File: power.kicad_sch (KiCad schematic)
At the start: 45 parts, among them U2 BQ25176J, U3 TPS61201DRC, U4 BQ51050BRHL

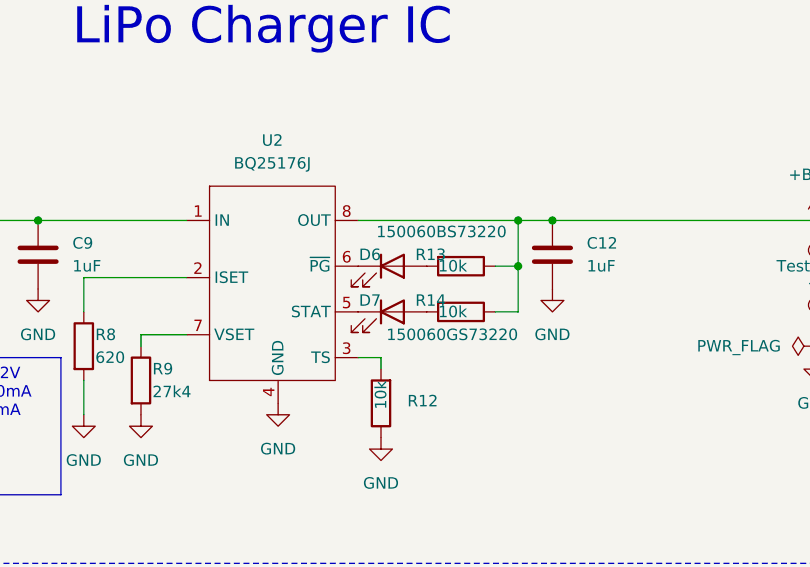
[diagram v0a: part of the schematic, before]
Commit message: change some more components to LCSC ones
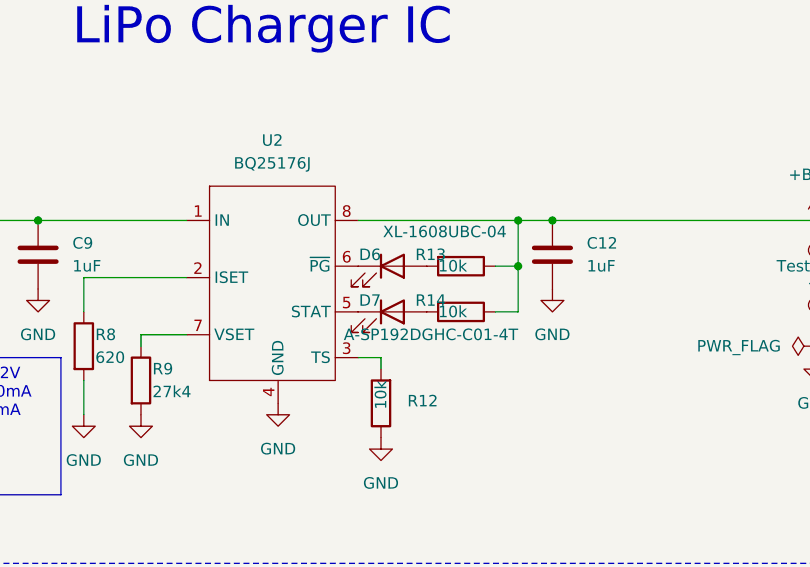
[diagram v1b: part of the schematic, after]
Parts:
- D6: value 150060BS73220 -> XL-1608UBC-04; mpn XL-1608UBC-04 -> C965807; part# 150060BS73220 -> C965807
- D7: value 150060GS73220 -> A-SP192DGHC-C01-4T; mpn A-SP192DGHC-C01-4T -> C19171301; part# 150060GS73220 -> C19171301
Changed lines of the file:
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@@
 			)
 		)
-		(property "Value" "150060BS73220"
+		(property "Value" "XL-1608UBC-04"
 			(at 91.44 121.92 0)
 			(effects
@@
 			)
 		)
-		(property "part#" "150060BS73220"
+		(property "part#" "C965807"
 			(at 78.74 125.73 0)
 			(effects
@@
 			)
 		)
-		(property "mpn" "XL-1608UBC-04"
+		(property "mpn" "C965807"
 			(at 78.74 125.73 0)
 			(effects
@@
 			)
 		)
-		(property "Value" "150060GS73220"
+		(property "Value" "A-SP192DGHC-C01-4T"
 			(at 92.71 133.35 0)
 			(effects
@@
 			)
 		)
-		(property "part#" "150060GS73220"
+		(property "part#" "C19171301"
 			(at 78.74 130.81 0)
 			(effects
@@
 			)
 		)
-		(property "mpn" "A-SP192DGHC-C01-4T"
+		(property "mpn" "C19171301"
 			(at 78.74 130.81 0)
 			(effects

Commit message: prepare for ordering
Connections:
- no-connect marks 1 -> 2
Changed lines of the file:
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@@
 		(at 181.61 67.31)
 	)
+	(no_connect
+		(at 207.01 90.17)
+	)
 	(wire
 		(pts
@@
 		(at 218.44 69.85 270)
 		(unit 1)
-		(exclude_from_sim no)
+		(exclude_from_sim yes)
 		(in_bom no)
 		(on_board no)
@@
 		(at 236.22 88.9 90)
 		(unit 1)
-		(exclude_from_sim no)
+		(exclude_from_sim yes)
 		(in_bom no)
 		(on_board no)
@@
 		(at 210.82 97.79 90)
 		(unit 1)
-		(exclude_from_sim no)
+		(exclude_from_sim yes)
 		(in_bom no)
 		(on_board no)
@@
 		(at 217.17 80.01 90)
 		(unit 1)
-		(exclude_from_sim no)
+		(exclude_from_sim yes)
 		(in_bom no)
 		(on_board no)
@@
 		(at 207.01 110.49 0)
 		(unit 1)
-		(exclude_from_sim no)
+		(exclude_from_sim yes)
 		(in_bom no)
 		(on_board no)
@@
 		(mirror x)
 		(unit 1)
-		(exclude_from_sim no)
+		(exclude_from_sim yes)
 		(in_bom no)
 		(on_board no)
@@
 		(at 176.53 78.74 90)
 		(unit 1)
-		(exclude_from_sim no)
+		(exclude_from_sim yes)
 		(in_bom no)
 		(on_board no)
@@
 		(at 176.53 82.55 90)
 		(unit 1)
-		(exclude_from_sim no)
+		(exclude_from_sim yes)
 		(in_bom no)
 		(on_board no)
@@
 		(at 214.63 100.33 0)
 		(unit 1)
-		(exclude_from_sim no)
+		(exclude_from_sim yes)
 		(in_bom no)
 		(on_board no)
@@
 		(at 207.01 105.41 180)
 		(unit 1)
-		(exclude_from_sim no)
+		(exclude_from_sim yes)
 		(in_bom no)
 		(on_board no)
@@
 		(at 194.31 107.95 0)
 		(unit 1)
-		(exclude_from_sim no)
+		(exclude_from_sim yes)
 		(in_bom no)
 		(on_board no)
@@
 		(at 220.98 100.33 0)
 		(unit 1)
-		(exclude_from_sim no)
+		(exclude_from_sim yes)
 		(in_bom no)
 		(on_board no)
@@
 		(at 173.99 90.17 180)
 		(unit 1)
-		(exclude_from_sim no)
+		(exclude_from_sim yes)
 		(in_bom no)
 		(on_board no)
@@
 		(at 210.82 69.85 0)
 		(unit 1)
-		(exclude_from_sim no)
+		(exclude_from_sim yes)
 		(in_bom no)
 		(on_board no)
@@
 		(at 227.33 67.31 0)
 		(unit 1)
-		(exclude_from_sim no)
+		(exclude_from_sim yes)
 		(in_bom no)
 		(on_board no)
@@
 		(at 165.1 85.09 90)
 		(unit 1)
-		(exclude_from_sim no)
+		(exclude_from_sim yes)
 		(in_bom no)
 		(on_board no)
@@
 		(at 165.1 87.63 90)
 		(unit 1)
-		(exclude_from_sim no)
+		(exclude_from_sim yes)
 		(in_bom no)
 		(on_board no)
@@
 		(at 218.44 67.31 90)
 		(unit 1)
-		(exclude_from_sim no)
+		(exclude_from_sim yes)
 		(in_bom no)
 		(on_board no)
@@
 		(mirror x)
 		(unit 1)
-		(exclude_from_sim no)
+		(exclude_from_sim yes)
 		(in_bom no)
 		(on_board no)
@@
 		(at 228.6 102.87 0)
 		(unit 1)
-		(exclude_from_sim no)
+		(exclude_from_sim yes)
 		(in_bom no)
 		(on_board no)
@@
 		(at 220.98 102.87 0)
 		(unit 1)
-		(exclude_from_sim no)
+		(exclude_from_sim yes)
 		(in_bom no)
 		(on_board no)
@@
 		(at 227.33 72.39 0)
 		(unit 1)
-		(exclude_from_sim no)
+		(exclude_from_sim yes)
 		(in_bom no)
 		(on_board no)
@@
 		(at 228.6 100.33 0)
 		(unit 1)
-		(exclude_from_sim no)
+		(exclude_from_sim yes)
 		(in_bom no)
 		(on_board no)
@@
 		(at 176.53 74.93 90)
 		(unit 1)
-		(exclude_from_sim no)
+		(exclude_from_sim yes)
 		(in_bom no)
 		(on_board no)
@@
 		(at 214.63 102.87 0)
 		(unit 1)
-		(exclude_from_sim no)
+		(exclude_from_sim yes)
 		(in_bom no)
 		(on_board no)
@@
 		(mirror x)
 		(unit 1)
-		(exclude_from_sim no)
+		(exclude_from_sim yes)
 		(in_bom no)
 		(on_board no)
@@
 		(at 213.36 80.01 270)
 		(unit 1)
-		(exclude_from_sim no)
+		(exclude_from_sim yes)
 		(in_bom no)
 		(on_board no)
@@
 		(at 157.48 90.17 180)
 		(unit 1)
-		(exclude_from_sim no)
+		(exclude_from_sim yes)
 		(in_bom no)
 		(on_board no)
@@
 		(at 176.53 90.17 180)
 		(unit 1)
-		(exclude_from_sim no)
+		(exclude_from_sim yes)
 		(in_bom no)
 		(on_board no)
@@
 		(at 228.6 93.98 0)
 		(unit 1)
-		(exclude_from_sim no)
+		(exclude_from_sim yes)
 		(in_bom no)
 		(on_board no)
@@
 		(at 213.36 92.71 270)
 		(unit 1)
-		(exclude_from_sim no)
+		(exclude_from_sim yes)
 		(in_bom no)
 		(on_board no)
@@
 		(at 194.31 85.09 0)
 		(unit 1)
-		(exclude_from_sim no)
+		(exclude_from_sim yes)
 		(in_bom no)
 		(on_board no)
@@
 		(at 233.68 88.9 270)
 		(unit 1)
-		(exclude_from_sim no)
+		(exclude_from_sim yes)
 		(in_bom no)
 		(on_board no)
@@
 		(at 181.61 69.85 270)
 		(unit 1)
-		(exclude_from_sim no)
+		(exclude_from_sim yes)
 		(in_bom no)
 		(on_board no)
@@
 		(at 227.33 76.2 0)
 		(unit 1)
-		(exclude_from_sim no)
+		(exclude_from_sim yes)
 		(in_bom no)
 		(on_board no)

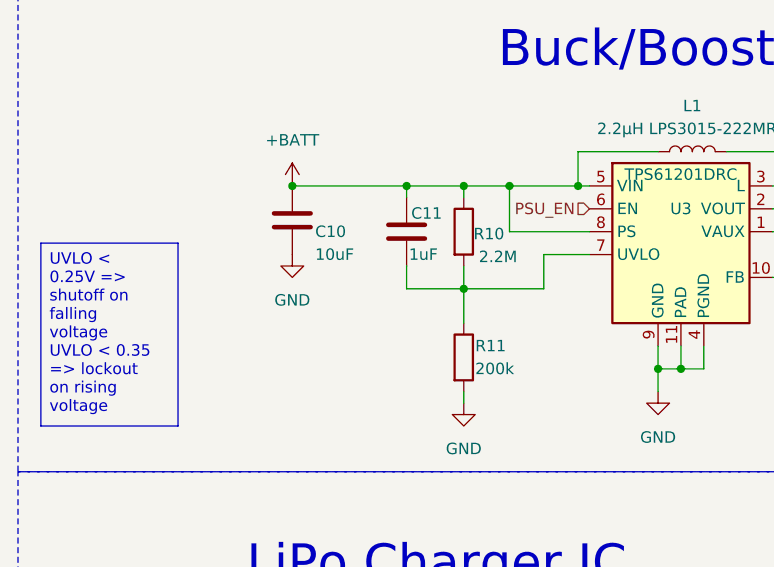
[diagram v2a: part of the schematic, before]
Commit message: begin improving power latching circuit
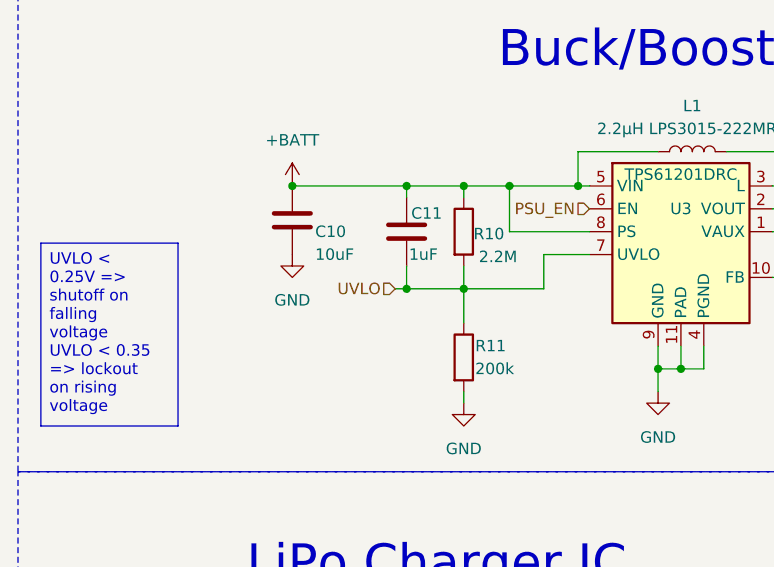
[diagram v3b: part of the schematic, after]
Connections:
- net UVLO: now reaches C11.2, R10.2, R11.1, U3.7 (UVLO)

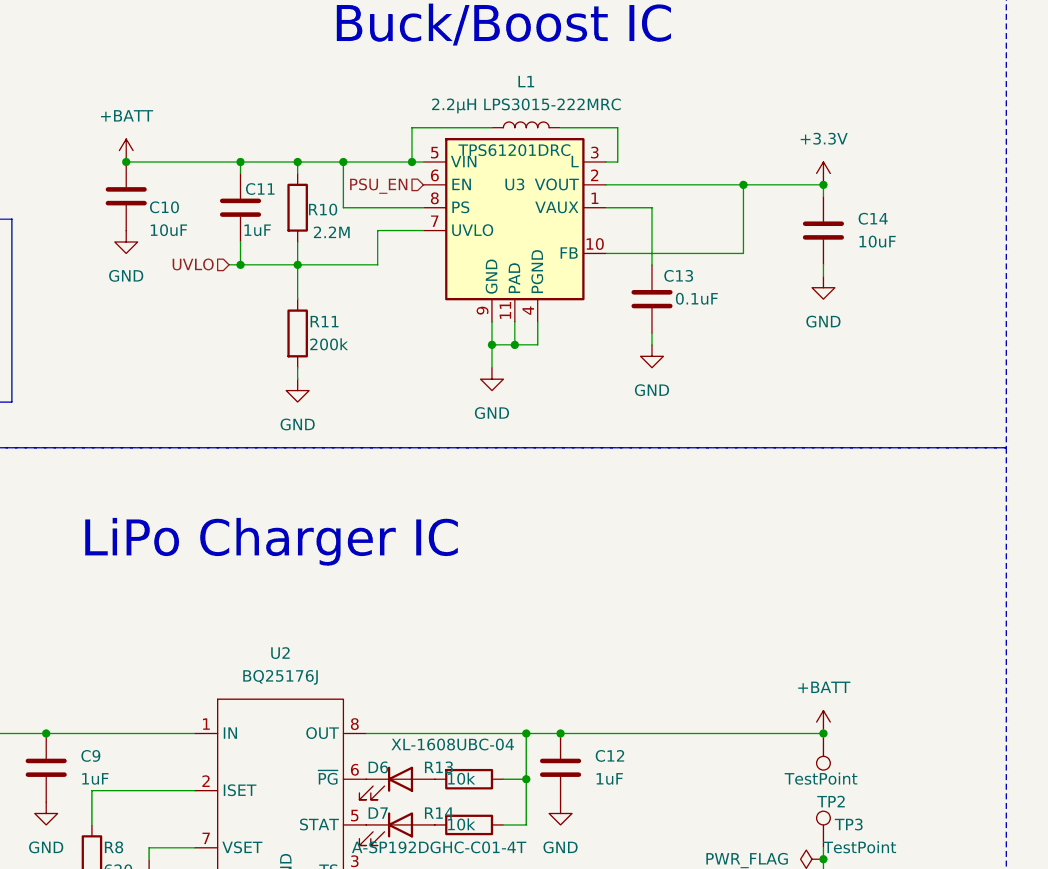
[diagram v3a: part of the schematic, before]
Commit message: change power ON and latching circuit to use FETs
should reduce leakage currents :)
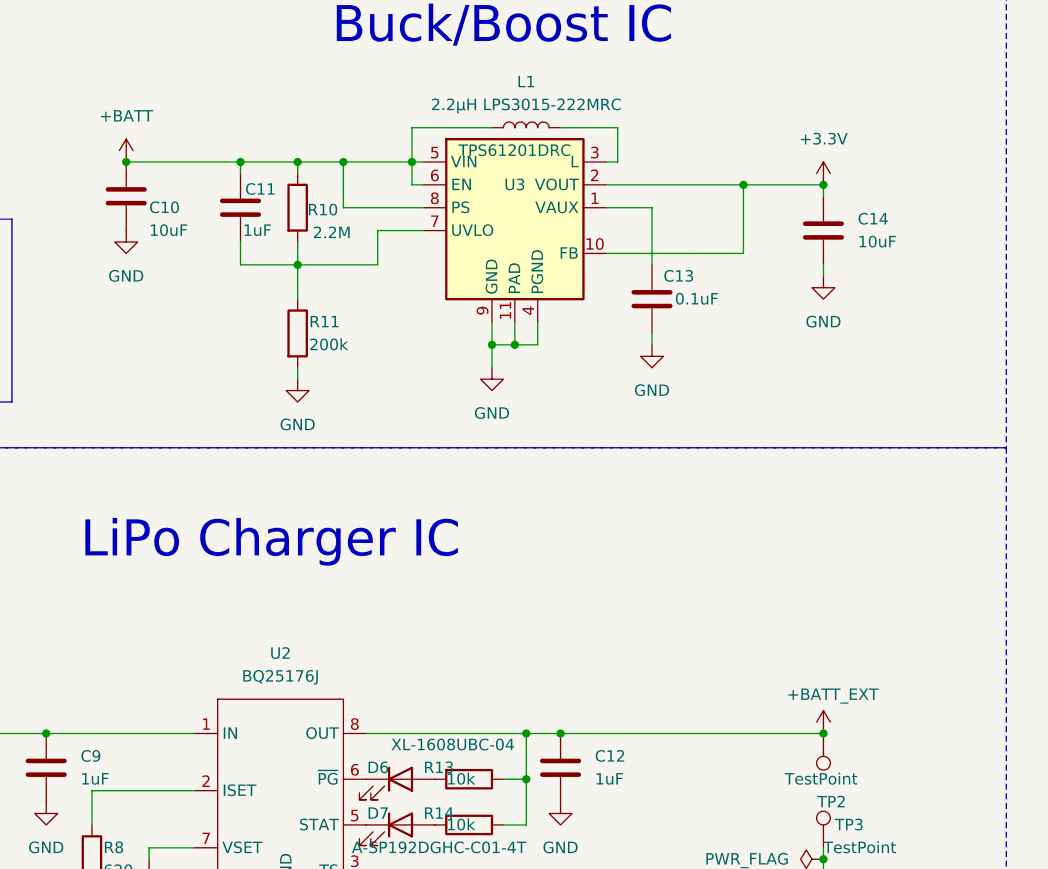
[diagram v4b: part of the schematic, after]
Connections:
- net PSU_EN is gone; now on net +BATT: U3.6 (EN)
- net +BATT: no longer C12.1, R13.1, R14.1, TP2.1, U2.8 (OUT)
- net UVLO: no longer names the net of C11.2, R10.2, R11.1, U3.7 (UVLO)
- new net +BATT_EXT: C12.1, R13.1, R14.1, TP2.1, U2.8 (OUT)
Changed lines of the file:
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@@
 	)
 	(junction
-		(at 60.96 68.58)
-		(diameter 0)
-		(color 0 0 0 0)
-	)
-	(junction
 		(at 67.31 68.58)
 		(diameter 0)
@@
 	)
 	(junction
-		(at 125.73 120.65)
-		(diameter 0)
-		(color 0 0 0 0)
-	)
-	(junction
 		(at 39.37 120.65)
 		(diameter 0)
@@
 	)
 	(junction
+		(at 125.73 120.65)
+		(diameter 0)
+		(color 0 0 0 0)
+	)
+	(junction
 		(at 227.33 67.31)
 		(diameter 0)
@@
 	(wire
 		(pts
+			(xy 80.01 59.69) (xy 80.01 57.15)
+		)
+		(stroke
+			(width 0)
+			(type default)
+		)
+	)
+	(wire
+		(pts
 			(xy 101.6 67.31) (xy 116.84 67.31)
 		)
@@
 	(wire
 		(pts
+			(xy 81.28 59.69) (xy 80.01 59.69)
+		)
+		(stroke
+			(width 0)
+			(type default)
+		)
+	)
+	(wire
+		(pts
 			(xy 173.99 82.55) (xy 173.99 85.09)
 		)
@@
 	(wire
 		(pts
-			(xy 59.69 68.58) (xy 60.96 68.58)
-		)
-		(stroke
-			(width 0)
-			(type default)
-		)
-	)
-	(wire
-		(pts
 			(xy 76.2 64.77) (xy 81.28 64.77)
 		)
@@
 		)
 	)
-	(hierarchical_label "PSU_EN"
-		(shape input)
-		(at 81.28 59.69 180)
-		(effects
-			(font
-				(size 1.27 1.27)
-			)
-			(justify right)
-		)
-	)
 	(hierarchical_label "Vcharge"
 		(shape input)
@@
 		)
 	)
-	(hierarchical_label "UVLO"
-		(shape input)
-		(at 59.69 68.58 180)
-		(effects
-			(font
-				(size 1.27 1.27)
-			)
-			(justify right)
-		)
-	)
 	(symbol
 		(lib_id "bier:TPS61201DRC")
@@
 	)
 	(symbol
-		(lib_id "power:+BATT")
-		(at 125.73 120.65 0)
-		(unit 1)
-		(exclude_from_sim no)
-		(in_bom yes)
-		(on_board yes)
-		(dnp no)
-		(fields_autoplaced yes)
-		(property "Reference" "#PWR052"
-			(at 125.73 124.46 0)
-			(effects
-				(font
-					(size 1.27 1.27)
-				)
-				(hide yes)
-			)
-		)
-		(property "Value" "+BATT"
-			(at 125.73 115.57 0)
-			(effects
-				(font
-					(size 1.27 1.27)
-				)
-			)
-		)
-		(property "Footprint" ""
-			(at 125.73 120.65 0)
-			(effects
-				(font
-					(size 1.27 1.27)
-				)
-				(hide yes)
-			)
-		)
-		(property "Datasheet" ""
-			(at 125.73 120.65 0)
-			(effects
-				(font
-					(size 1.27 1.27)
-				)
-				(hide yes)
-			)
-		)
-		(property "Description" "Power symbol creates a global label with name \"+BATT\""
-			(at 125.73 120.65 0)
-			(effects
-				(font
-					(size 1.27 1.27)
-				)
-				(hide yes)
-			)
-		)
-		(pin "1"
-		)
-		(instances
-			(project ""
-				(path "/a4ffe097-37ef-4e19-a91a-ae57f4a5aad1/06d9cd17-cb19-4cdd-8e67-c41d1b4a676e"
-					(reference "#PWR052")
-					(unit 1)
-				)
-			)
-		)
-	)
-	(symbol
 		(lib_id "Device:C")
 		(at 125.73 64.77 0)
@@
 					(unit 1)
 				)
+			)
+		)
+	)
+	(symbol
+		(lib_id "power:+BATT")
+		(at 125.73 120.65 0)
+		(unit 1)
+		(exclude_from_sim no)
+		(in_bom yes)
+		(on_board yes)
+		(dnp no)
+		(property "Reference" "#PWR052"
+			(at 125.73 124.46 0)
+			(effects
+				(font
+					(size 1.27 1.27)
+				)
+				(hide yes)
+			)
+		)
+		(property "Value" "+BATT_EXT"
+			(at 126.746 116.332 0)
+			(effects
+				(font
+					(size 1.27 1.27)
+				)
+			)
+		)
+		(property "Footprint" ""
+			(at 125.73 120.65 0)
+			(effects
+				(font
+					(size 1.27 1.27)
+				)
+				(hide yes)
+			)
+		)
+		(property "Datasheet" ""
+			(at 125.73 120.65 0)
+			(effects
+				(font
+					(size 1.27 1.27)
+				)
+				(hide yes)
+			)
+		)
+		(property "Description" "Power symbol creates a global label with name \"+BATT\""
+			(at 125.73 120.65 0)
+			(effects
+				(font
+					(size 1.27 1.27)
+				)
+				(hide yes)
+			)
+		)
+		(pin "1"
+		)
+		(instances
+			(project "bierdeckel"
+				(path "/a4ffe097-37ef-4e19-a91a-ae57f4a5aad1/06d9cd17-cb19-4cdd-8e67-c41d1b4a676e"
+					(reference "#PWR052")
+					(unit 1)
+				)

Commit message: add info in license to PCB design
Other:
- title: (none) -> Bierdeckel
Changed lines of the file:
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@@
 	(generator_version "9.0")
 	(paper "A4")
+	(title_block
+		(title "Bierdeckel")
+		(rev "0.4")
+		(comment 1 "SPDX-License-Identifier: CERN-OHL-S-2.0")
+		(comment 2 "SPDX-FileCopyrightText: 2023-2025 Stefan Riesenberger <stefan.riesenberger@gmail.com>")
+	)
 	(rectangle
 		(start 17.78 34.29)
